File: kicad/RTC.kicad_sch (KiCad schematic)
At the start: 14 parts, among them J5 Conn_01x02_Pin, Q6 PMOS, U6 PCF8523T, Y1 ABS07AIG-32.768KHZ-7-T

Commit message: pre ERC
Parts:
- added TP24: INT_G, project footprints:TestPoint_THTPad_D2.0mm_Drill1.0mm, symbol Connector:TestPoint
- added TP25: INT_D, project footprints:TestPoint_THTPad_D2.0mm_Drill1.0mm, symbol Connector:TestPoint
- C23: renamed from C15; footprint (none) -> Capacitor_SMD:C_0805_2012Metric_Pad1.18x1.45mm_HandSolder; MPN (none) -> (Generic); Manufacturer (none) -> (Generic); Package (none) -> 0805; Subsystem (none) -> 07-RTC; Supplier 1 (none) -> (Generic)
- C24: renamed from C16; footprint (none) -> Capacitor_SMD:C_0805_2012Metric_Pad1.18x1.45mm_HandSolder; MPN (none) -> (Generic); Manufacturer (none) -> (Generic); Package (none) -> 0805; Subsystem (none) -> 07-RTC; Supplier 1 (none) -> (Generic)
- C25: renamed from C12; footprint (none) -> Capacitor_SMD:C_0805_2012Metric_Pad1.18x1.45mm_HandSolder; MPN (none) -> (Generic); Manufacturer (none) -> (Generic); Package (none) -> 0805; Subsystem (none) -> 07-RTC; Supplier 1 (none) -> (Generic)
- D10: Subsystem 06-MCU-IO -> 07-RTC
- J9: renamed from J5; footprint (none) -> Connector_PinHeader_2.54mm:PinHeader_1x02_P2.54mm_Vertical; Subsystem (none) -> 07-RTC
- JP21: renamed from JP19; Subsystem (none) -> 07-RTC
- JP22: renamed from JP23; Subsystem (none) -> 07-RTC
- JP23: renamed from JP22; Subsystem (none) -> 07-RTC
- Q6: Subsystem 01-Power-Mux -> 07-RTC
- R41: renamed from R23; Manufacturer (none) -> (Generic); Package (none) -> 0805; Subsystem (none) -> 07-RTC; Supplier 1 (none) -> (Generic)
- R42: renamed from R25; Manufacturer (none) -> (Generic); Subsystem 06-MCU-IO -> 07-RTC; Supplier 1 (none) -> (Generic)
- R43: renamed from R40; Manufacturer (none) -> (Generic); Package (none) -> 0805; Subsystem (none) -> 07-RTC; Supplier 1 (none) -> (Generic)
- U7: renamed from U6; MPN (none) -> PCF8523T/1,118; Manufacturer (none) -> NXP; Package (none) -> SOP-8; Subsystem (none) -> 07-RTC; Supplier 1 (none) -> LCSC; Supplier 1 SKU (none) -> C2651516; Supplier 1 URL (none) -> https://lcsc.com/product-detail/Real-Time-Clocks_NXP-PCF852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
- Y2: renamed from Y1; footprint (none) -> Crystal:Crystal_SMD_3215-2Pin_3.2x1.5mm; Subsystem (none) -> 07-RTC
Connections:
- net at JP23.1 (A), Q6.1 (D): now also TP25.1
- net INT_G: now reaches D10.1 (K), JP21.2 (B), JP22.2 (B), Q6.2 (G), R43.1
- net INT_G: now also TP24.1
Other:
- note added: "For Pullups see MCU sheet"
- note removed: "Probe CLKOut with 10:1 probe with JP10 = Open"
- moved on the sheet: C23, C24, C25, D10, J9, JP21, JP22, JP23, Q6, R41, R42, R43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

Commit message: ERC done
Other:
- moved on the sheet: C23, C24

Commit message: layout floorplanning
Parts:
- C23, C24, C25: footprint Capacitor_SMD:C_0805_2012Metric_Pad1.18x1.45mm_HandSolder -> Capacitor_SMD:C_0603_1608Metric_Pad1.08x0.95mm_HandSolder; Package 0805 -> 0603
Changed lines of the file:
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@@
 			)
 		)
-		(property "Footprint" "Capacitor_SMD:C_0805_2012Metric_Pad1.18x1.45mm_HandSolder"
+		(property "Footprint" "Capacitor_SMD:C_0603_1608Metric_Pad1.08x0.95mm_HandSolder"
 			(at 119.38 92.4052 0)
 			(effects
@@
 			)
 		)
-		(property "Package" "0805"
+		(property "Package" "0603"
 			(at 123.19 91.44 90)
 			(effects
@@
 			)
 		)
-		(property "Footprint" "Capacitor_SMD:C_0805_2012Metric_Pad1.18x1.45mm_HandSolder"
+		(property "Footprint" "Capacitor_SMD:C_0603_1608Metric_Pad1.08x0.95mm_HandSolder"
 			(at 135.5852 66.04 0)
 			(effects
@@
 			)
 		)
-		(property "Package" "0805"
+		(property "Package" "0603"
 			(at 134.62 62.23 0)
 			(effects
@@
 			)
 		)
-		(property "Footprint" "Capacitor_SMD:C_0805_2012Metric_Pad1.18x1.45mm_HandSolder"
+		(property "Footprint" "Capacitor_SMD:C_0603_1608Metric_Pad1.08x0.95mm_HandSolder"
 			(at 145.7452 66.04 0)
 			(effects
@@
 			)
 		)
-		(property "Package" "0805"
+		(property "Package" "0603"
 			(at 144.78 62.23 0)
 			(effects

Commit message: layout rtc
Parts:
- removed C23: 2.2u, Capacitor_SMD:C_0603_1608Metric_Pad1.08x0.95mm_HandSolder, symbol Device:C
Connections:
- net VDD_IN: now reaches C25.1, R41.1, U7.8 (VDD)
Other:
- moved on the sheet: C24, R41

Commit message: floorplanning
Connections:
- net CLKOUT renamed INT_CLKOUT
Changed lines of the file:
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@@
 		)
 	)
-	(label "CLKOUT"
+	(label "INT_CLKOUT"
 		(at 147.32 105.41 0)
 		(effects

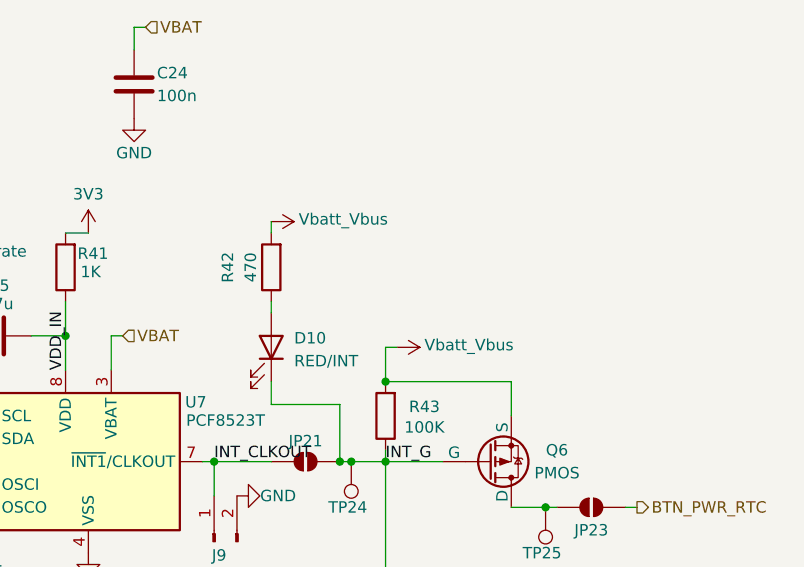
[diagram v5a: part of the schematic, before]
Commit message: layout - footprints update - may have corrupted kicad_sch project lib
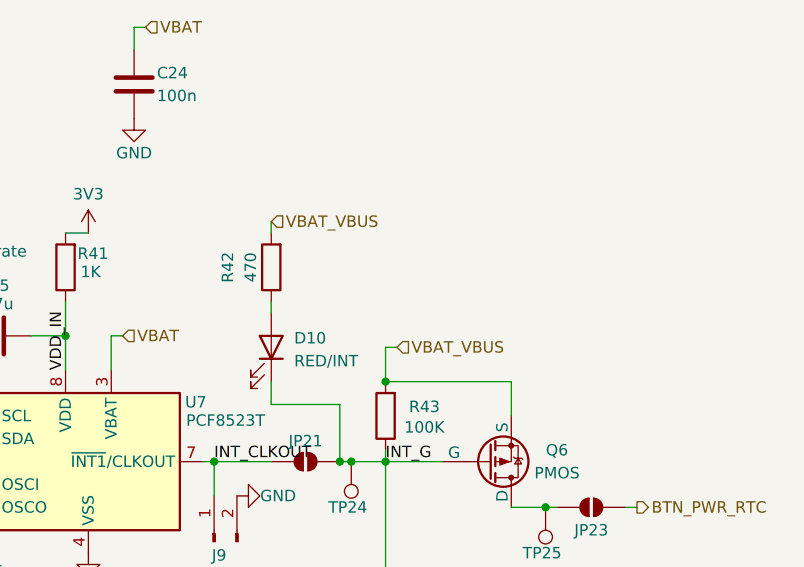
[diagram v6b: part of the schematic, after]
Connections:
- net Vbatt_Vbus renamed VBAT_VBUS
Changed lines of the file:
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@@
+		)
+	)
+	(hierarchical_label "VBAT_VBUS"
+		(shape input)
+		(at 167.64 92.71 0)
+		(effects
+			(font
+				(size 1.27 1.27)
+			)
+			(justify left)
 		)
 	)
@@
 		(shape output)
 		(at 189.23 120.65 0)
+		(effects
+			(font
+				(size 1.27 1.27)
+			)
+			(justify left)
+		)
+	)
+	(hierarchical_label "VBAT_VBUS"
+		(shape input)
+		(at 153.67 78.74 0)
 		(effects
 			(font
@@
 	)
 	(symbol
-		(lib_id "power:VDD")
-		(at 167.64 92.71 270)
-		(mirror x)
-		(unit 1)
-		(exclude_from_sim no)
-		(in_bom yes)
-		(on_board yes)
-		(dnp no)
-		(property "Reference" "#PWR071"
-			(at 163.83 92.71 0)
-			(effects
-				(font
-					(size 1.27 1.27)
-				)
-				(hide yes)
-			)
-		)
-		(property "Value" "Vbatt_Vbus"
-			(at 170.688 92.456 90)
-			(effects
-				(font
-					(size 1.27 1.27)
-				)
-				(justify left)
-			)
-		)
-		(property "Footprint" ""
-			(at 167.64 92.71 0)
-			(effects
-				(font
-					(size 1.27 1.27)
-				)
-				(hide yes)
-			)
-		)
-		(property "Datasheet" ""
-			(at 167.64 92.71 0)
-			(effects
-				(font
-					(size 1.27 1.27)
-				)
-				(hide yes)
-			)
-		)
-		(property "Description" ""
-			(at 167.64 92.71 0)
-			(effects
-				(font
-					(size 1.27 1.27)
-				)
-				(hide yes)
-			)
-		)
-		(pin "1"
-		)
-		(instances
-			(project "10k-Hour-Timer-RP2040"
-				(path "/9d26b66f-2a94-42e5-8460-016e0bf95186/0e234469-901c-4318-947f-74f6fef01c6d"
-					(reference "#PWR071")
-					(unit 1)
-				)
-			)
-		)
-	)
-	(symbol
 		(lib_id "Jumper:SolderJumper_2_Open")
 		(at 189.23 110.49 0)
@@
 					(unit 1)
 				)
-			)
-		)
-	)
-	(symbol
-		(lib_id "power:VDD")
-		(at 153.67 78.74 270)
-		(mirror x)
-		(unit 1)
-		(exclude_from_sim no)
-		(in_bom yes)
-		(on_board yes)
-		(dnp no)
-		(property "Reference" "#PWR070"
-			(at 149.86 78.74 0)
-			(effects
-				(font
-					(size 1.27 1.27)
-				)
-				(hide yes)
-			)
-		)
-		(property "Value" "Vbatt_Vbus"
-			(at 156.718 78.486 90)
-			(effects
-				(font
-					(size 1.27 1.27)
-				)
-				(justify left)
-			)
-		)
-		(property "Footprint" ""
-			(at 153.67 78.74 0)
-			(effects
-				(font
-					(size 1.27 1.27)
-				)
-				(hide yes)
-			)
-		)
-		(property "Datasheet" ""
-			(at 153.67 78.74 0)
-			(effects
-				(font
-					(size 1.27 1.27)
-				)
-				(hide yes)
-			)
-		)
-		(property "Description" ""
-			(at 153.67 78.74 0)
-			(effects
-				(font
-					(size 1.27 1.27)
-				)
-				(hide yes)
-			)
-		)
-		(pin "1"
-		)
-		(instances
-			(project "10k-Hour-Timer-RP2040"
-				(path "/9d26b66f-2a94-42e5-8460-016e0bf95186/0e234469-901c-4318-947f-74f6fef01c6d"
-					(reference "#PWR070")
-					(unit 1)
-				)

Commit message: changed usb port, prepare first bom export
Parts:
- C24, C25, J9: Lab_In_Stock (none) -> Y
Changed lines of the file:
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@@
+			)
+		)
+		(property "Lab_In_Stock" "Y"
+			(at 123.19 91.44 90)
+			(effects
+				(font
+					(size 1.27 1.27)
+				)
+				(hide yes)
 			)
 		)
@@
 		)
 		(property "Supplier 1" "(Generic)"
+			(at 138.43 63.5 0)
+			(effects
+				(font
+					(size 1.27 1.27)
+				)
+				(hide yes)
+			)
+		)
+		(property "Lab_In_Stock" "Y"
 			(at 138.43 63.5 0)
 			(effects
@@
 			(at 147.32 114.3 90)
 			(effects
+				(font
+					(size 1.27 1.27)
+				)
+				(hide yes)
+			)
+		)
+		(property "Lab_In_Stock" "Y"
+			(at 147.32 114.3 90)
+			(effects

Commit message: production files for PCBWay initial - BOM manually edited for PCBA
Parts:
- J9: now not fitted
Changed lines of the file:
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@@
 		(in_bom yes)
 		(on_board yes)
-		(dnp no)
+		(dnp yes)
 		(property "Reference" "J9"
 			(at 147.066 115.824 90)
